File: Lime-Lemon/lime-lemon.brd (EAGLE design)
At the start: 94 x 88 mm, 66 parts

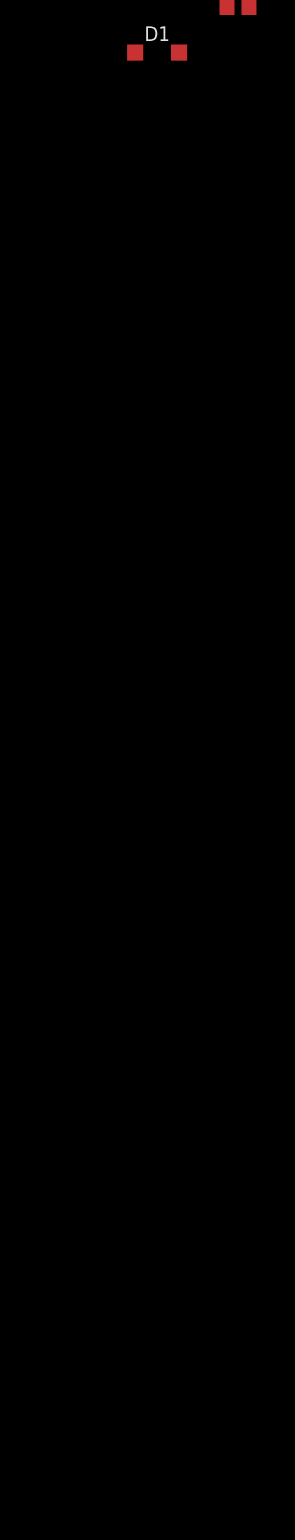
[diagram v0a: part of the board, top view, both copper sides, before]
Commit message: Add new lime-lemon board, schematic and inductor library
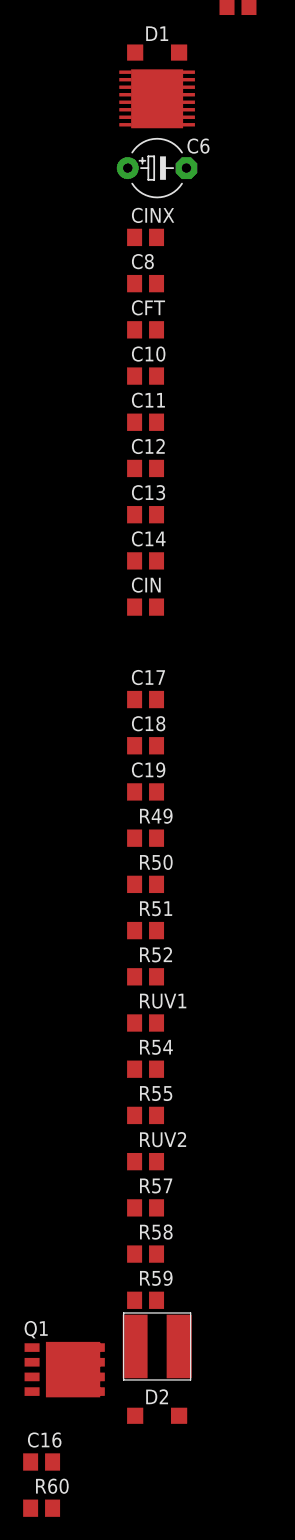
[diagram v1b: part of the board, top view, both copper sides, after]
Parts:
- added C10, C11, C12, C13, C14, C16, C17, C18, C19: (no value), rcl:C0805
- added C6: (no value), rcl:E5-5
- added C8: 1u, rcl:C0805
- added CFT: 68n, rcl:C0805
- added CIN: 1uF, rcl:C0805
- added CINX: 100n, rcl:C0805
- added D2: (no value), diode:SOD123
- added Q1: BSZ105N04NS, transistor-power:PG-TDSON-8
- added R49, R51, R52, R54, R55, R57, R58, R59: (no value), rcl:R0805
- added R50: 1.5k, rcl:R0805
- added R60: 150, rcl:R0805
- added RUV1: 3.57k, rcl:R0805
- added RUV2: 10k, rcl:R0805
- added U$2: LM5088, Klick_custom_lm5088:LM5088
- added U$3: KLICK_INDUCTOR01, Klick_inductor01:KLICK_INDUCTOR01
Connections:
- new net N$43: CFT.1, RUV1.2, RUV2.1, U$2.P$2
- new net N$45: C13.1, U$2.P$3
- new net N$48: C14.1, R49.1, U$2.P$9
- new net N$52: C11.1, R49.2, R51.2
- new net N$53: R51.1, U$2.P$4
- new net N$54: R52.2, U$2.P$5
- new net N$55: C16.1, U$2.P$15
- new net N$56: C18.1, R55.1
- new net N$57: C18.2, C19.2, R57.1, R58.1, R59.2, R60.1, U$2.P$8
- new net N$58: C19.1, R55.2, U$2.P$7
- new net N$59: C10.1, U$2.P$10
- new net N$60: R54.2, U$2.P$13
- new net N$61: C10.2, D2.C, Q1.1, Q1.2, Q1.3, U$2.P$12, U$3.P$2
- new net N$62: R50.1, R60.2
- new net N$65: Q1.4, U$2.P$11
- new net N$71: C12.2, R58.2
- net +5V: now also C8.1, CIN.1, CINX.1, Q1.5, Q1.6, Q1.7, Q1.8, Q1.TH, RUV2.2, U$2.P$1
- net GND: now also C17.1, C6.+, CIN.2, CINX.2, U$3.P$1
- net VDD: now also C11.2, C12.1, C13.2, C14.2, C16.2, C17.2, C6.-, C8.2, CFT.2, D2.A, R50.2, R52.1, R59.1, RUV1.1, U$2.P$14, U$2.P$16, U$2.P$6
